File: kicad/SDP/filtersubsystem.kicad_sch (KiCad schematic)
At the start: 9 parts

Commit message: Added sheet
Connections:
- net +24V renamed +12V
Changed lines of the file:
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@@
     (pin "2")
-  )
-  (symbol (lib_id "power:+24V") (at 82.55 29.21 0) (unit 1)
-    (in_bom yes) (on_board yes)
-    (property "Reference" "#PWR?" (id 0) (at 82.55 33.02 0)
-      (effects (font (size 1.27 1.27)) hide)
-    )
-    (property "Value" "+24V" (id 1) (at 83.82 24.13 0))
-    (property "Footprint" "" (id 2) (at 82.55 29.21 0)
-      (effects (font (size 1.27 1.27)) hide)
-    )
-    (property "Datasheet" "" (id 3) (at 82.55 29.21 0)
-      (effects (font (size 1.27 1.27)) hide)
-    )
-    (pin "1")
   )
   (symbol (lib_id "power:GND") (at 82.55 38.1 0) (unit 1)
@@
       (effects (font (size 1.27 1.27)) hide)
     )
+    (pin "1")
+  )
+  (symbol (lib_id "power:+12V") (at 82.55 29.21 0) (unit 1)
+    (in_bom yes) (on_board yes) (fields_autoplaced)
+    (property "Reference" "#PWR?" (id 0) (at 82.55 33.02 0)
+      (effects (font (size 1.27 1.27)) hide)
+    )
+    (property "Value" "+12V" (id 1) (at 82.55 24.13 0))
+    (property "Footprint" "" (id 2) (at 82.55 29.21 0)
+      (effects (font (size 1.27 1.27)) hide)
+    )
+    (property "Datasheet" "" (id 3) (at 82.55 29.21 0)
+      (effects (font (size 1.27 1.27)) hide)
+    )

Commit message: Updated schematics
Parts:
- added A? (x2): Pololu_Breakout_A4988, Module:Pololu_Breakout-16_15.2x20.3mm, symbol Driver_Motor:Pololu_Breakout_A4988
- added C? (x2): 100u, symbol Device:C_Small
- added J? (x2): Conn_01x04, symbol Connector_Generic:Conn_01x04
- added JP? (x2): JP_MS1, symbol Jumper:Jumper_2_Open
- added JP? (x2): JP_MS3, symbol Jumper:Jumper_2_Open
- added JP? (x2): JP_MS2, symbol Jumper:Jumper_2_Open
- added R? (x4): 10k, symbol Device:R_Small
- added R? (x2): 100k, symbol Device:R_Small
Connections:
- net +12V: now also A?.8 (VMOT), A?.8 (VMOT), C?.1, C?.1
- net +3V3: now also A?.2 (VDD), A?.2 (VDD), JP?.1 (A), JP?.1 (A), JP?.1 (A), JP?.1 (A), JP?.1 (A), JP?.1 (A)
- net GND: now also A?.1 (GND), A?.1 (GND), A?.7 (GND), A?.7 (GND), C?.2, C?.2, R?.1, R?.1, R?.2, R?.2, R?.2, R?.2
- net P59_!EN renamed P76_EN
- net P76_EN: now also A?.9 (~{ENABLE})
- net P87_STEP renamed P77_STEP
- net P77_STEP: now also A?.15 (STEP), R?.1
- net P88_DIR renamed P78_DIR
- net P78_DIR: now also A?.16 (DIR), R?.1
- new net: A?.10 (MS1), JP?.2 (B), R?.2 (x2)
- new net: A?.11 (MS2), JP?.2 (B) (x2)
- new net: A?.12 (MS3), JP?.2 (B) (x2)
- new net: A?.13 (~{RESET}), A?.14 (~{SLEEP}) (x2)
- new net: A?.3 (1B), J?.1 (Pin_1) (x2)
- new net: A?.4 (1A), J?.2 (Pin_2) (x2)
- new net: A?.5 (2A), J?.3 (Pin_3) (x2)
- new net: A?.6 (2B), J?.4 (Pin_4) (x2)
- new net P79_EN: A?.9 (~{ENABLE})
- new net P80_STEP: A?.15 (STEP), R?.1
- new net P81_DIR: A?.16 (DIR), R?.1
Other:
- note added: "Fan Axis"
- note added: "Filter Silo Elevation"

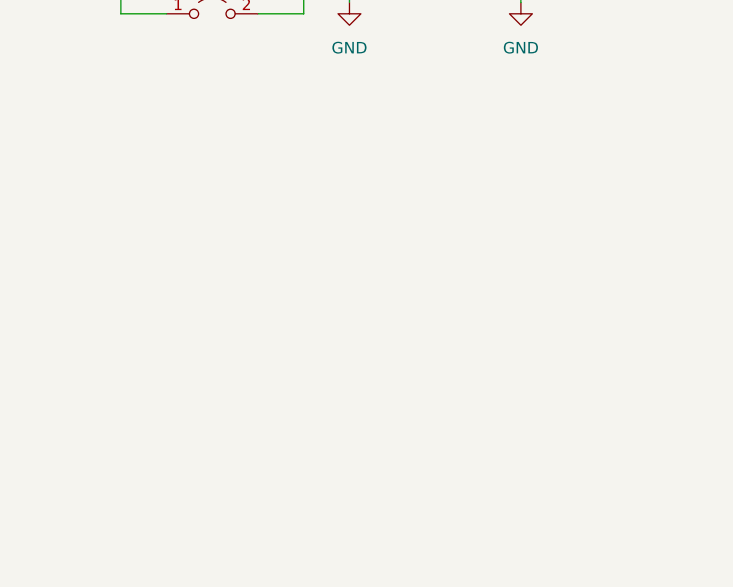
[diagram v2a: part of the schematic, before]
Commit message: Added DS3231 RTC and HM-10 BLE module
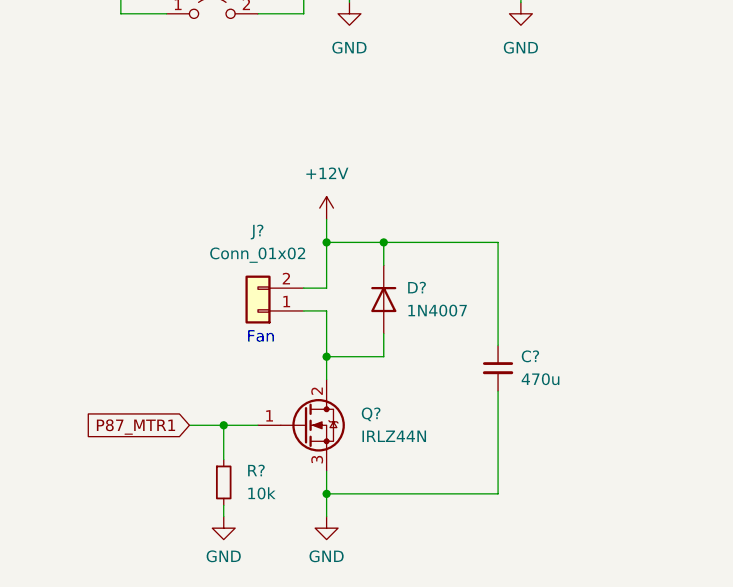
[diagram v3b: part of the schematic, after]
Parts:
- added C?: 470u, symbol Device:C_Small
- added D?: 1N4007, Diode_THT:D_DO-41_SOD81_P10.16mm_Horizontal, symbol Diode:1N4007
- added J?: Conn_01x02, symbol Connector_Generic:Conn_01x02
- added Q?: IRLZ44N, Package_TO_SOT_THT:TO-220-3_Vertical, symbol Transistor_FET:IRLZ44N
- added R?: 10k, symbol Device:R_Small
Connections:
- net +12V: now also C?.1, D?.1 (K), J?.2 (Pin_2)
- net GND: now also C?.2, Q?.3 (S), R?.2
- new net: D?.2 (A), J?.1 (Pin_1), Q?.2 (D)
- new net P87_MTR1: Q?.1 (G), R?.1
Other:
- note added: "Fan"

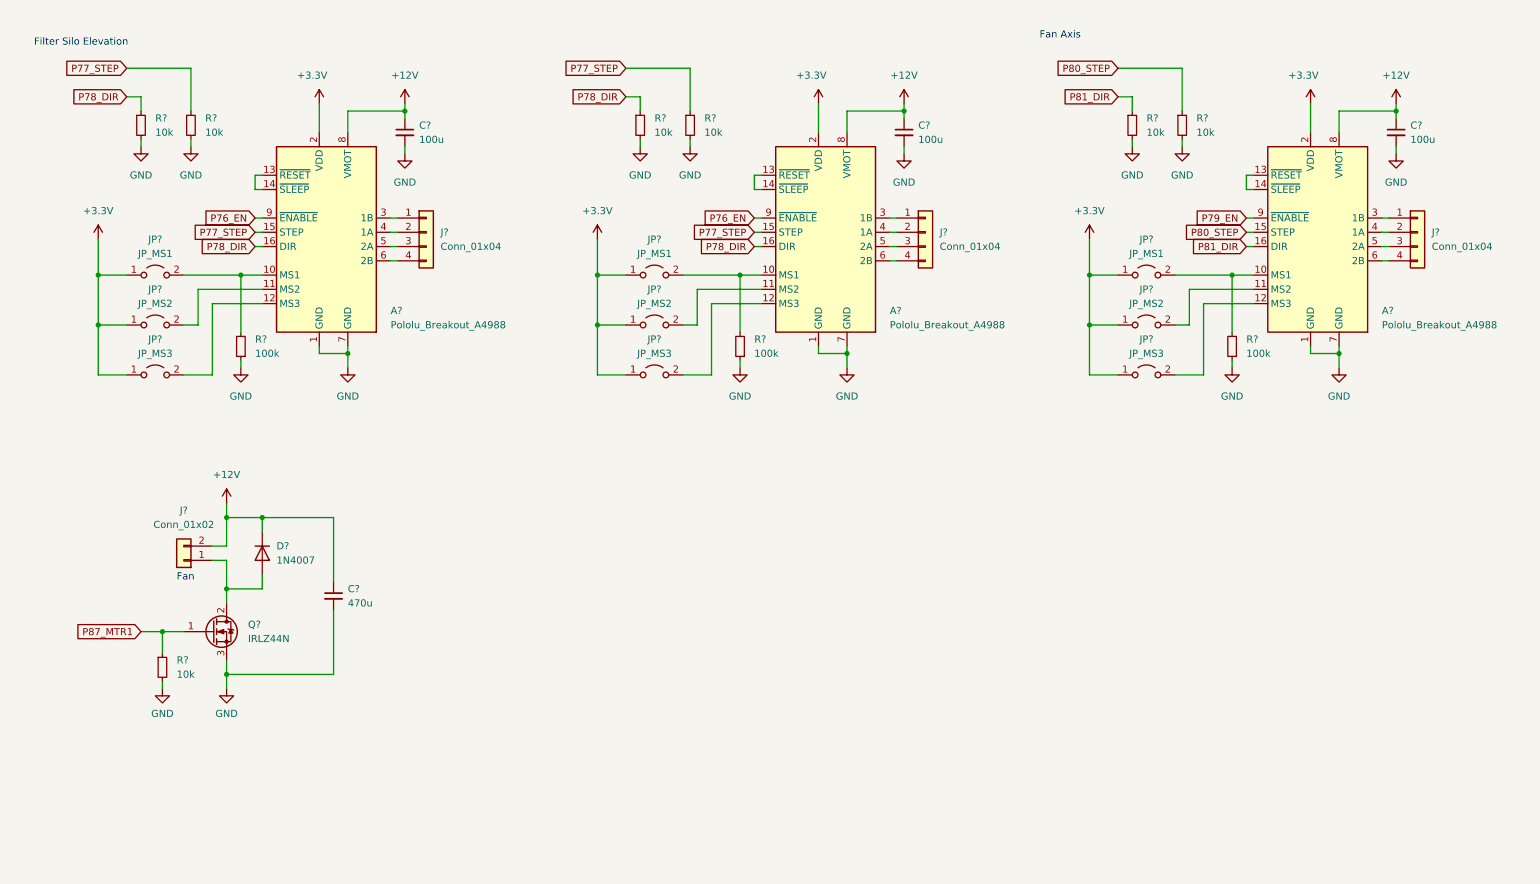
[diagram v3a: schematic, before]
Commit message: Added GPIO headers, separated power PCB
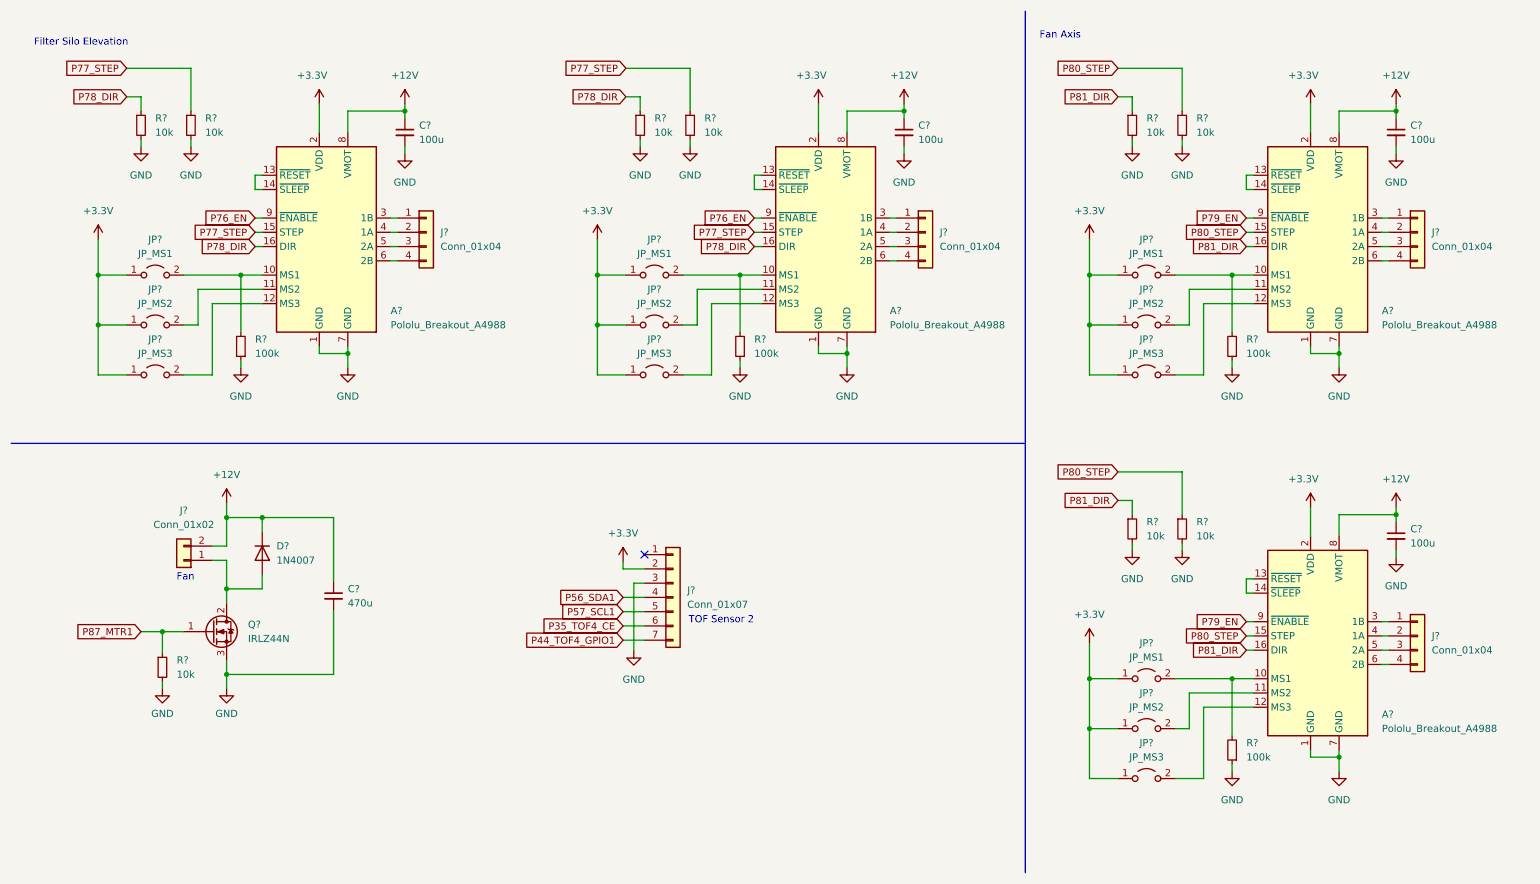
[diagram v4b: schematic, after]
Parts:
- added A?: Pololu_Breakout_A4988, Module:Pololu_Breakout-16_15.2x20.3mm, symbol Driver_Motor:Pololu_Breakout_A4988
- added C?: 100u, symbol Device:C_Small
- added J?: Conn_01x07, symbol Connector_Generic:Conn_01x07
- added J?: Conn_01x04, symbol Connector_Generic:Conn_01x04
- added JP?: JP_MS3, symbol Jumper:Jumper_2_Open
- added JP?: JP_MS1, symbol Jumper:Jumper_2_Open
- added JP?: JP_MS2, symbol Jumper:Jumper_2_Open
- added R? (x2): 10k, symbol Device:R_Small
- added R?: 100k, symbol Device:R_Small
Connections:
- net +12V: now also A?.8 (VMOT), C?.1
- net +3V3: now also A?.2 (VDD), J?.2 (Pin_2), JP?.1 (A), JP?.1 (A), JP?.1 (A)
- net GND: now also A?.1 (GND), A?.7 (GND), C?.2, J?.3 (Pin_3), R?.1, R?.2, R?.2
- net P79_EN: now also A?.9 (~{ENABLE})
- net P80_STEP: now also A?.15 (STEP), R?.1
- net P81_DIR: now also A?.16 (DIR), R?.1
- new net: A?.10 (MS1), JP?.2 (B), R?.2
- new net: A?.12 (MS3), JP?.2 (B)
- new net: A?.11 (MS2), JP?.2 (B)
- new net: A?.13 (~{RESET}), A?.14 (~{SLEEP})
- new net: A?.3 (1B), J?.1 (Pin_1)
- new net: A?.4 (1A), J?.2 (Pin_2)
- new net: A?.5 (2A), J?.3 (Pin_3)
- new net: A?.6 (2B), J?.4 (Pin_4)
- new net P35_TOF4_CE: J?.6 (Pin_6)
- new net P44_TOF4_GPIO1: J?.7 (Pin_7)
- new net P56_SDA1: J?.4 (Pin_4)
- new net P57_SCL1: J?.5 (Pin_5)
- no-connect marks 0 -> 1
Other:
- note added: "TOF Sensor 2"

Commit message: Added footprints
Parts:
- gave numbers to parts that had none: 42

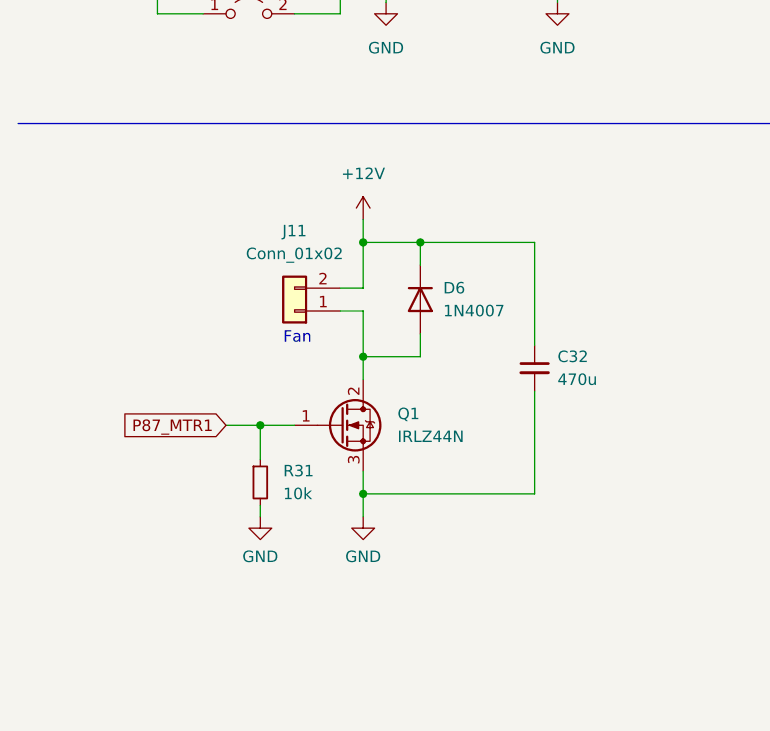
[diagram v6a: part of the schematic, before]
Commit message: Added footprints
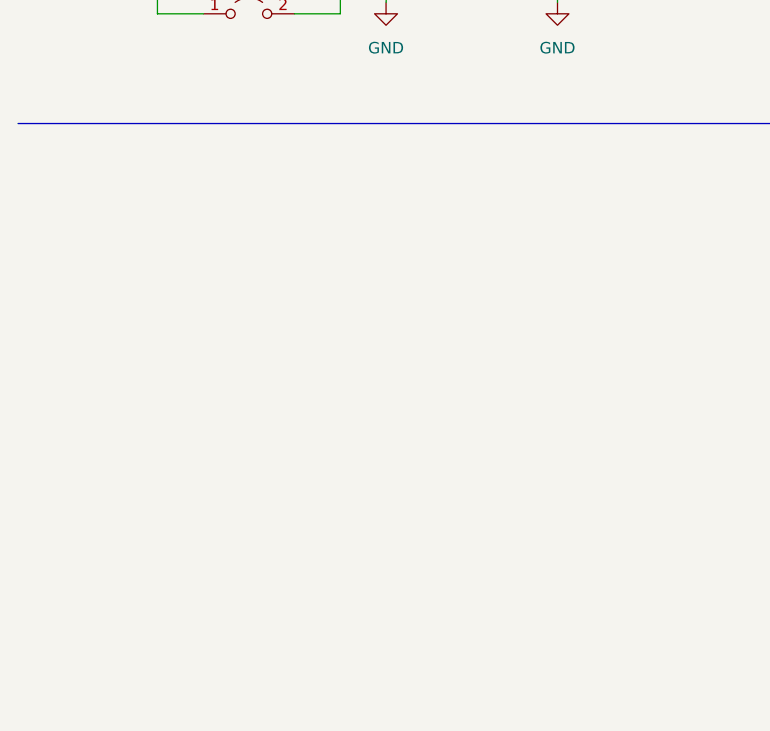
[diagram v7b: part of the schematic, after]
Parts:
- removed C32: 470u, symbol Device:C_Small
- removed D6: 1N4007, Diode_THT:D_DO-41_SOD81_P10.16mm_Horizontal, symbol Diode:1N4007
- removed J11: Conn_01x02, symbol Connector_Generic:Conn_01x02
- removed Q1: IRLZ44N, Package_TO_SOT_THT:TO-220-3_Vertical, symbol Transistor_FET:IRLZ44N
- removed R31: 10k, symbol Device:R_Small
- C28, C29, C30, C31: footprint (none) -> footprints:50TZV100M8X10.5
- R20, R21, R22, R23, R24, R25, R26, R27, R28, R29, R30, R32: footprint (none) -> Resistor_SMD:R_0805_2012Metric
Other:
- note removed: "Fan"

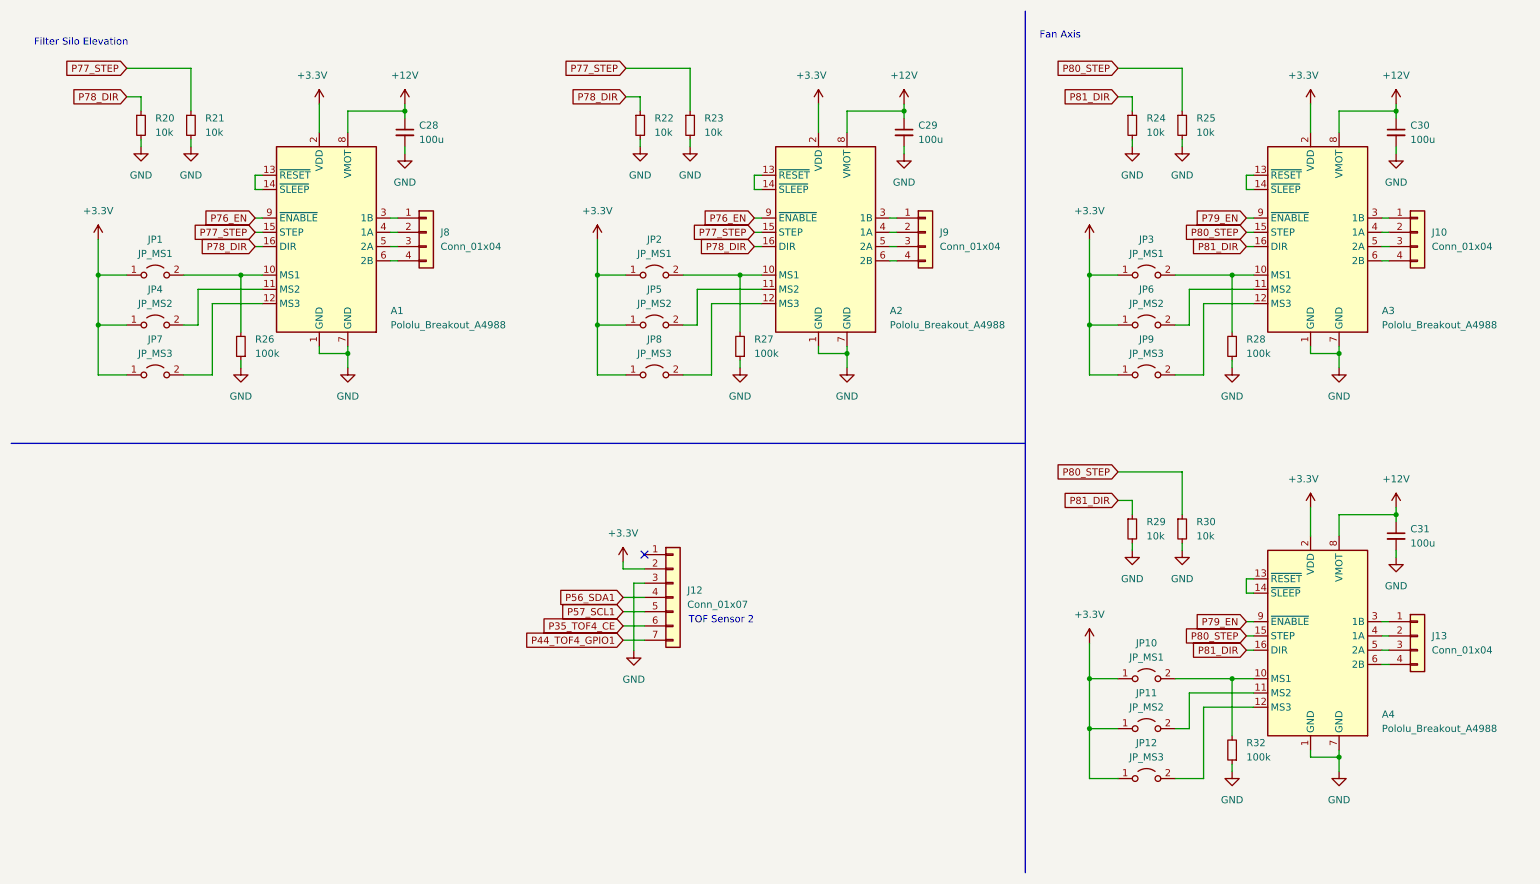
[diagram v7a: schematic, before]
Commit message: Assigned footprints, added limit switches, rearranged schematics
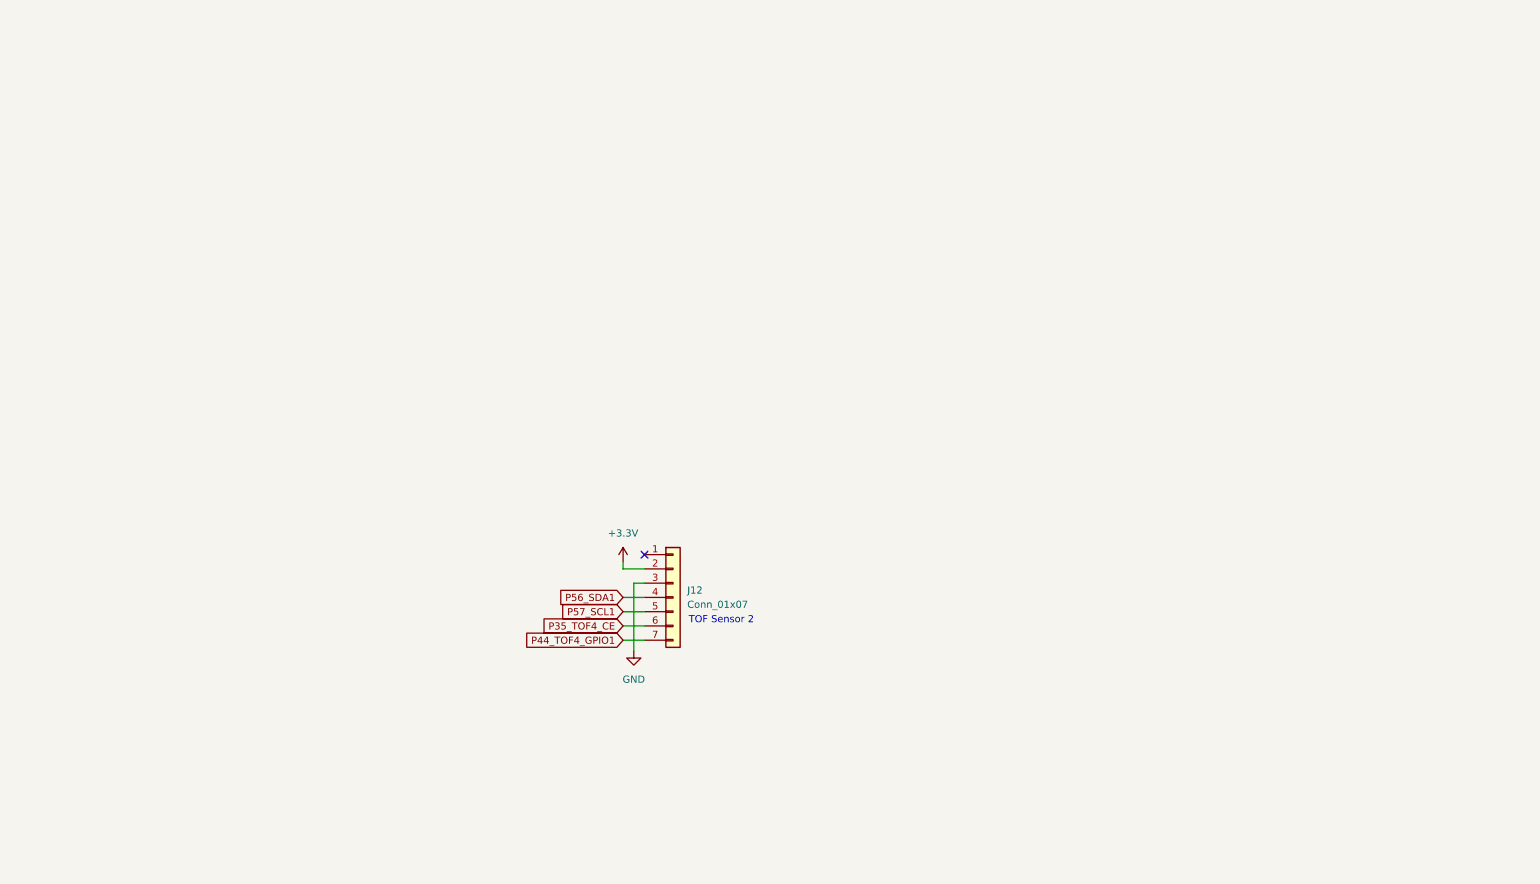
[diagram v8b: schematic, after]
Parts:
- removed A1, A2, A3, A4: Pololu_Breakout_A4988, Module:Pololu_Breakout-16_15.2x20.3mm, symbol Driver_Motor:Pololu_Breakout_A4988
- removed C28, C29, C30, C31: 100u, footprints:50TZV100M8X10.5, symbol Device:C_Small
- removed J10, J13, J8, J9: Conn_01x04, symbol Connector_Generic:Conn_01x04
- removed JP1, JP10, JP2, JP3: JP_MS1, symbol Jumper:Jumper_2_Open
- removed JP11, JP4, JP5, JP6: JP_MS2, symbol Jumper:Jumper_2_Open
- removed JP12, JP7, JP8, JP9: JP_MS3, symbol Jumper:Jumper_2_Open
- removed R20, R21, R22, R23, R24, R25, R29, R30: 10k, Resistor_SMD:R_0805_2012Metric, symbol Device:R_Small
- removed R26, R27, R28, R32: 100k, Resistor_SMD:R_0805_2012Metric, symbol Device:R_Small
- J12: footprint (none) -> Connector_PinSocket_2.54mm:PinSocket_1x07_P2.54mm_Vertical
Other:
- note removed: "Fan Axis"
- note removed: "Filter Silo Elevation"
